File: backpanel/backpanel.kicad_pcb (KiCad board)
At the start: 2 copper layers, 103 x 30.5 mm, 10 parts

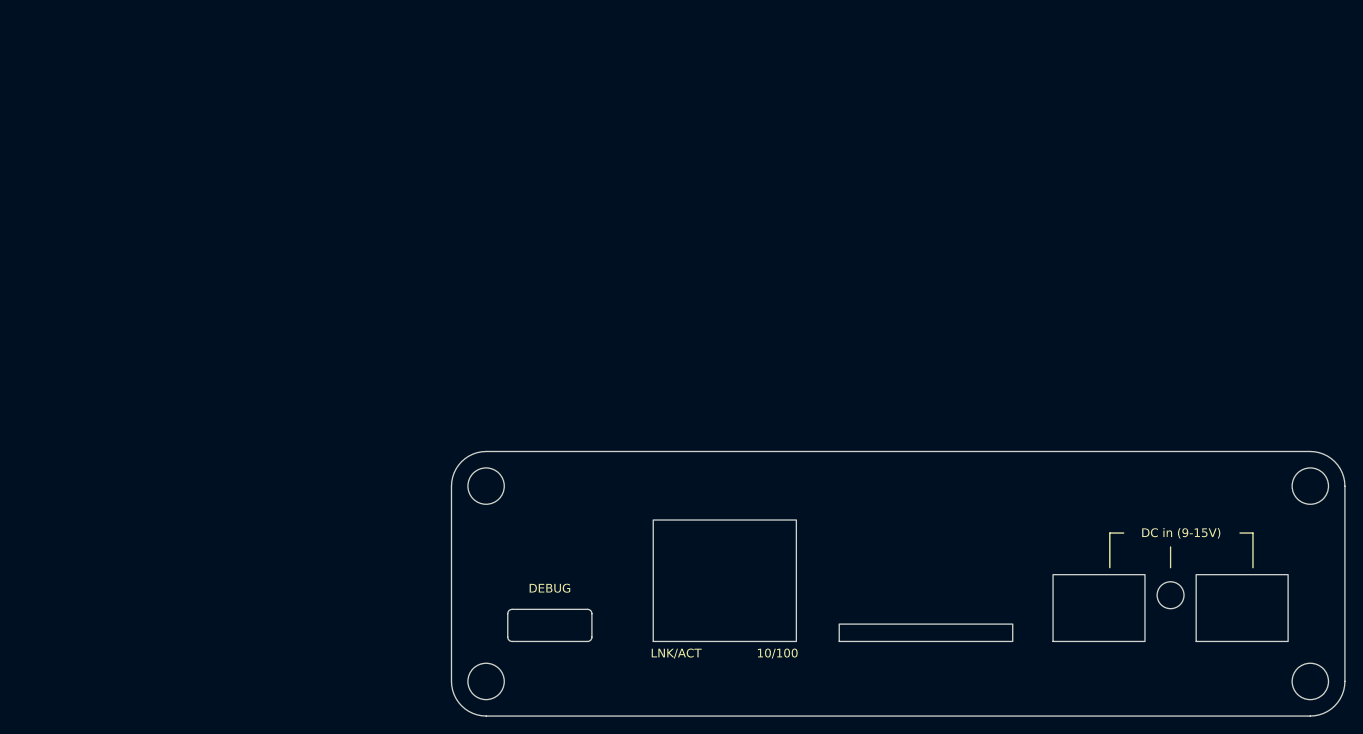
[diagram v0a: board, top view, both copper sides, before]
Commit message: Add 3d models
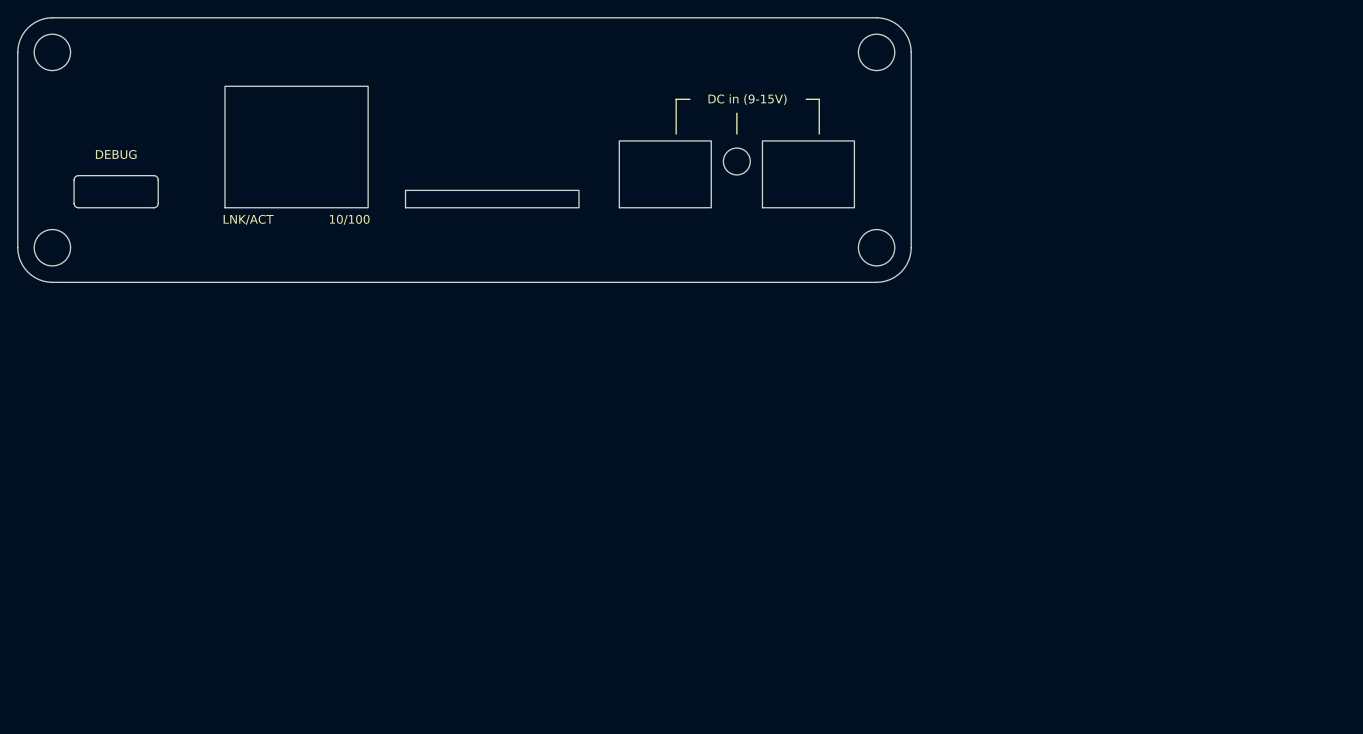
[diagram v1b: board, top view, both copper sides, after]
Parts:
- moved REF** 70.7 mm to (11.3, 21.9)
- moved REF** 70.7 mm to (27.7, 21.9)
- moved REF** 70.7 mm to (91.3, 21.9)
- moved REF** 70.7 mm to (54.7, 21.9)
- moved REF** 70.7 mm to (3.99, 26.5)
- moved REF** 70.7 mm to (3.99, 3.99)
- moved REF** 70.7 mm to (74.8, 21.9)
- moved REF** 70.7 mm to (82.9, 21.6)
- moved ? 70.7 mm to (99.0, 26.5)
- moved ? 70.7 mm to (99.0, 3.99)
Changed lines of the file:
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@@
       (layerselection 0x00010fc_ffffffff)
       (disableapertmacros false)
-      (usegerberextensions false)
+      (usegerberextensions true)
       (usegerberattributes true)
       (usegerberadvancedattributes true)
-      (creategerberjobfile true)
+      (creategerberjobfile false)
       (svguseinch false)
       (svgprecision 6)
@@
       (outputformat 1)
       (mirror false)
-      (drillshape 1)
+      (drillshape 0)
       (scaleselection 1)
-      (outputdirectory "")
+      (outputdirectory "fab")
     )
   )
   (net 0 "")
   (footprint "Frontpanel:USB-C_C167321" (layer "F.Cu")
-    (at 61.34 71.9)
+    (at 11.34 21.9)
     (fp_text reference "REF**" (at 0 1.85 unlocked) (layer "F.SilkS") hide
       (effects (font (size 1 1) (thickness 0.15)))
@@
   )
   (footprint "Frontpanel:Connector_RJ45_HR911105A_C12074" (layer "F.Cu")
-    (at 77.7 71.9)
+    (at 27.7 21.9)
     (fp_text reference "REF**" (at 0 -0.5 unlocked) (layer "F.SilkS") hide
       (effects (font (size 1 1) (thickness 0.15)))
@@
     )
     (fp_line (start 0 0) (end 0 -5) (layer "Eco1.User") (width 0.05))
-    (fp_rect (start -4.44 0) (end 12.06 -14) (layer "Edge.Cuts") (width 0.12) (fill none))
+    (fp_rect (start -3.81 0) (end 12.69 -14) (layer "Edge.Cuts") (width 0.12) (fill none))
   )
   (footprint "Frontpanel:BarrelJack_C963204" (layer "F.Cu")
-    (at 141.35 71.9)
+    (at 91.35 21.9)
     (fp_text reference "REF**" (at 0 -0.5 unlocked) (layer "F.SilkS") hide
       (effects (font (size 1 1) (thickness 0.15)))
@@
   )
   (footprint "" (layer "F.Cu")
-    (at 149.01 76.51)
+    (at 99.01 26.51)
     (fp_text reference "" (at 0 0) (layer "F.SilkS")
       (effects (font (size 1.27 1.27) (thickness 0.15)))
@@
   )
   (footprint "Frontpanel:ESP32_WROOM_32E_C701342" (layer "F.Cu")
-    (at 104.7 71.9)
+    (at 54.7 21.9)
     (fp_text reference "REF**" (at 0 -0.5 unlocked) (layer "F.SilkS") hide
       (effects (font (size 1 1) (thickness 0.15)))
@@
   )
   (footprint "" (layer "F.Cu")
-    (at 149.01 53.99)
+    (at 99.01 3.99)
     (fp_text reference "" (at 0 0) (layer "F.SilkS")
       (effects (font (size 1.27 1.27) (thickness 0.15)))
@@
   )
   (footprint "Frontpanel:Hole_0.165in" (layer "F.Cu")
-    (at 53.99 76.51)
+    (at 3.99 26.51)
     (fp_text reference "REF**" (at 0 -0.5 unlocked) (layer "F.SilkS") hide
       (effects (font (size 1 1) (thickness 0.15)))
@@
   )
   (footprint "Frontpanel:Hole_0.165in" (layer "F.Cu")
-    (at 53.99 53.99)
+    (at 3.99 3.99)
     (fp_text reference "REF**" (at 0 -0.5 unlocked) (layer "F.SilkS") hide
       (effects (font (size 1 1) (thickness 0.15)))
@@
   )
   (footprint "Frontpanel:BarrelJack_C397334" (layer "F.Cu")
-    (at 124.85 71.9)
+    (at 74.85 21.9)
     (fp_text reference "REF**" (at 0 -0.5 unlocked) (layer "F.SilkS") hide
       (effects (font (size 1 1) (thickness 0.15)))
@@
   )
   (footprint "Frontpanel:IndicatorLED_C417352" (layer "F.Cu")
-    (at 132.9 71.65)
+    (at 82.9 21.65)
     (fp_text reference "REF**" (at 0 -0.5 unlocked) (layer "F.SilkS") hide
       (effects (font (size 1 1) (thickness 0.15)))
@@
     (pad "" np_thru_hole circle (at 0 -5.08) (size 3.1 3.1) (drill 3.1) (layers *.Mask))
   )
-  (gr_line (start 142.4 63.4) (end 142.4 59.4) (layer "F.SilkS") (width 0.15))
-  (gr_line (start 142.4 59.4) (end 140.9 59.4) (layer "F.SilkS") (width 0.15))
-  (gr_line (start 132.9 63.4) (end 132.9 61) (layer "F.SilkS") (width 0.15))
-  (gr_line (start 125.9 63.4) (end 125.9 59.4) (layer "F.SilkS") (width 0.15))
-  (gr_line (start 125.9 59.4) (end 127.5 59.4) (layer "F.SilkS") (width 0.15))
-  (gr_rect (start 50 50) (end 153 80.5) (layer "Eco1.User") (width 0.1) (fill none))
-  (gr_arc (start 50 54) (mid 51.171573 51.171573) (end 54 50) (layer "Edge.Cuts") (width 0.1))
-  (gr_line (start 50 76.5) (end 50 54) (layer "Edge.Cuts") (width 0.1))
-  (gr_line (start 149 50) (end 54 50) (layer "Edge.Cuts") (width 0.1))
-  (gr_line (start 149 80.5) (end 54 80.5) (layer "Edge.Cuts") (width 0.1))
-  (gr_arc (start 153 76.5) (mid 151.828427 79.328427) (end 149 80.5) (layer "Edge.Cuts") (width 0.1))
-  (gr_arc (start 149 50) (mid 151.828427 51.171573) (end 153 54) (layer "Edge.Cuts") (width 0.1))
-  (gr_line (start 153 54) (end 153 76.5) (layer "Edge.Cuts") (width 0.1))
-  (gr_arc (start 54 80.5) (mid 51.171573 79.328427) (end 50 76.5) (layer "Edge.Cuts") (width 0.1))
-  (gr_text "JLCJLCJLCJLC" (at 101.5 56) (layer "B.SilkS")
+  (gr_line (start 92.4 13.4) (end 92.4 9.4) (layer "F.SilkS") (width 0.15))
+  (gr_line (start 92.4 9.4) (end 90.9 9.4) (layer "F.SilkS") (width 0.15))
+  (gr_line (start 82.9 13.4) (end 82.9 11) (layer "F.SilkS") (width 0.15))
+  (gr_line (start 75.9 13.4) (end 75.9 9.4) (layer "F.SilkS") (width 0.15))
+  (gr_line (start 75.9 9.4) (end 77.5 9.4) (layer "F.SilkS") (width 0.15))
+  (gr_rect (start 0 0) (end 103 30.5) (layer "Eco1.User") (width 0.1) (fill none))
+  (gr_arc (start 0 4) (mid 1.171573 1.171573) (end 4 0) (layer "Edge.Cuts") (width 0.1))
+  (gr_line (start 0 26.5) (end 0 4) (layer "Edge.Cuts") (width 0.1))
+  (gr_line (start 99 0) (end 4 0) (layer "Edge.Cuts") (width 0.1))
+  (gr_line (start 99 30.5) (end 4 30.5) (layer "Edge.Cuts") (width 0.1))
+  (gr_arc (start 103 26.5) (mid 101.828427 29.328427) (end 99 30.5) (layer "Edge.Cuts") (width 0.1))
+  (gr_arc (start 99 0) (mid 101.828427 1.171573) (end 103 4) (layer "Edge.Cuts") (width 0.1))
+  (gr_line (start 103 4) (end 103 26.5) (layer "Edge.Cuts") (width 0.1))
+  (gr_arc (start 4 30.5) (mid 1.171573 29.328427) (end 0 26.5) (layer "Edge.Cuts") (width 0.1))
+  (gr_text "JLCJLCJLCJLC" (at 51.5 6) (layer "B.SilkS")
     (effects (font (size 1 1) (thickness 0.15)) (justify mirror))
   )
-  (gr_text "LNK/ACT" (at 72.95 73.275) (layer "F.SilkS")
+  (gr_text "LNK/ACT" (at 23.6 23.275) (layer "F.SilkS")
     (effects (font (size 1 1) (thickness 0.15)) (justify left))
   )
-  (gr_text "DC in (9-15V)" (at 134.125 59.4) (layer "F.SilkS")
+  (gr_text "DC in (9-15V)" (at 84.125 9.4) (layer "F.SilkS")
     (effects (font (size 1 1) (thickness 0.15)))
   )
-  (gr_text "DEBUG" (at 61.34 65.8) (layer "F.SilkS")
+  (gr_text "DEBUG" (at 11.34 15.8) (layer "F.SilkS")
     (effects (font (size 1 1) (thickness 0.15)))
   )
-  (gr_text "10/100" (at 90 73.275) (layer "F.SilkS")
+  (gr_text "10/100" (at 40.65 23.275) (layer "F.SilkS")
     (effects (font (size 1 1) (thickness 0.15)) (justify right))
   )
